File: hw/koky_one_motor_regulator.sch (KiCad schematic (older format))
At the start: 15 parts, among them CON1 ISP-MLW-6, SW1 Rotary_Encoder_Switch, U1 ATMEGA328P-PU, U2 StepStick, Y1 16MHz

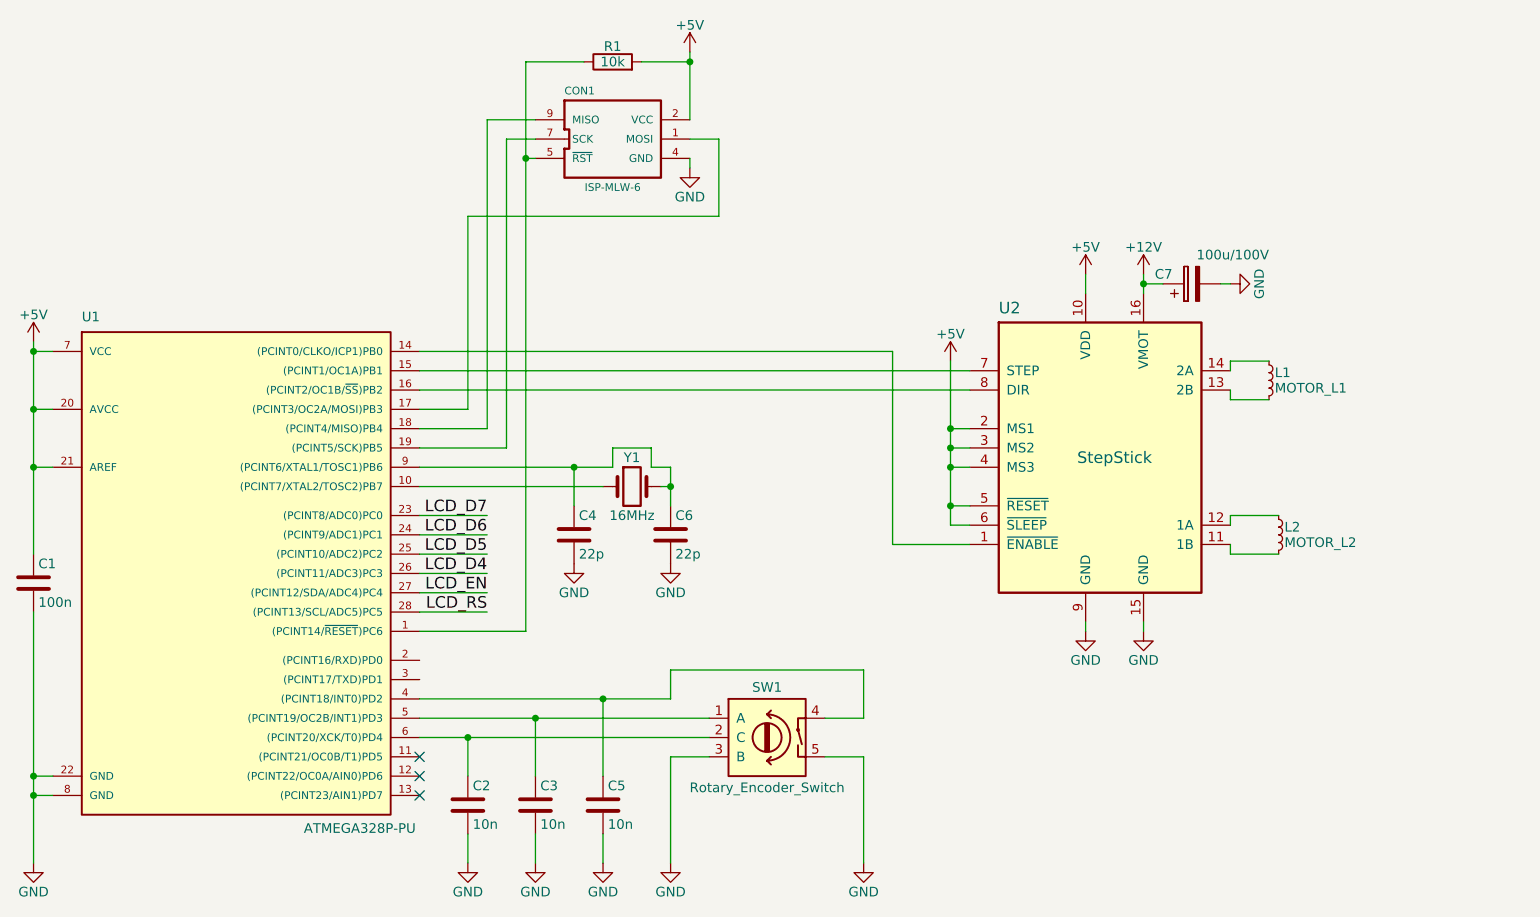
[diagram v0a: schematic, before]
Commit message: v2
Zlepšení časování, vylepšení TUI, změna zapojení
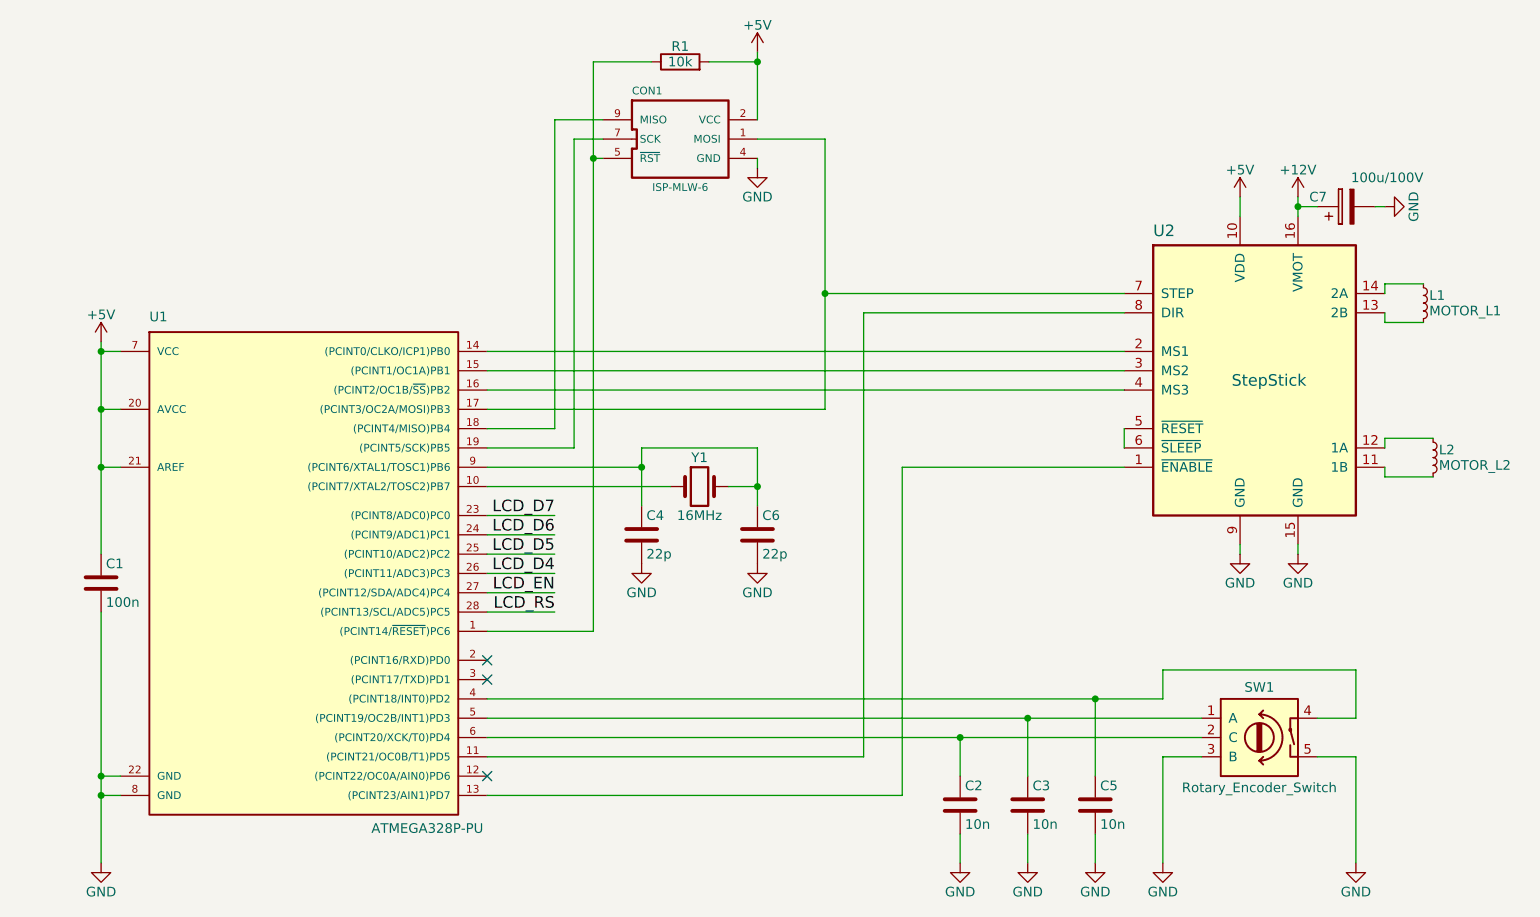
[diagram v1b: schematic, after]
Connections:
- net +5V: no longer U2.2 (MS1), U2.3 (MS2), U2.4 (MS3), U2.5 (~RESET), U2.6 (~SLEEP)
- net at U1.11 ((PCINT21/OC0B/T1)PD5): now also U2.8 (DIR)
- net at U1.13 ((PCINT23/AIN1)PD7): now also U2.1 (~ENABLE)
- net at U1.14 ((PCINT0/CLKO/ICP1)PB0): now also U2.2 (MS1); no longer U2.1 (~ENABLE)
- net at U1.15 ((PCINT1/OC1A)PB1): now also U2.3 (MS2); no longer U2.7 (STEP)
- net at U1.16 ((PCINT2/OC1B/~SS~)PB2): now also U2.4 (MS3); no longer U2.8 (DIR)
- net at CON1.1 (MOSI), U1.17 ((PCINT3/OC2A/MOSI)PB3): now also U2.7 (STEP)
- new net: U2.5 (~RESET), U2.6 (~SLEEP)
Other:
- moved on the sheet: C1, C2, C3, C4, C5, C6, C7, CON1, L1, L2, R1, SW1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
